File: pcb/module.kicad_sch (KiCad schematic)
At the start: 2 parts, among them J3 Conn_02x07_Counter_Clockwise

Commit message: worked on power
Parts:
- removed A1: RaspberryPi_Pico, Module:RaspberryPi_Pico_SMD_HandSolder, symbol MCU_Module:RaspberryPi_Pico_Debug
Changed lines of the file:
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@@
-		)
-	)
-	(symbol
-		(lib_id "MCU_Module:RaspberryPi_Pico_Debug")
-		(at 210.82 63.5 0)
-		(unit 1)
-		(body_style 1)
-		(exclude_from_sim no)
-		(in_bom yes)
-		(on_board yes)
-		(in_pos_files yes)
-		(dnp no)
-		(fields_autoplaced yes)
-		(property "Reference" "A1"
-			(at 212.9633 97.79 0)
-			(show_name no)
-			(do_not_autoplace no)
-			(effects
-				(font
-					(size 1.27 1.27)
-				)
-				(justify left)
-			)
-		)
-		(property "Value" "RaspberryPi_Pico"
-			(at 212.9633 100.33 0)
-			(show_name no)
-			(do_not_autoplace no)
-			(effects
-				(font
-					(size 1.27 1.27)
-				)
-				(justify left)
-			)
-		)
-		(property "Footprint" "Module:RaspberryPi_Pico_SMD_HandSolder"
-			(at 210.82 110.49 0)
-			(hide yes)
-			(show_name no)
-			(do_not_autoplace no)
-			(effects
-				(font
-					(size 1.27 1.27)
-				)
-			)
-		)
-		(property "Datasheet" "https://datasheets.raspberrypi.com/pico/pico-datasheet.pdf"
-			(at 210.82 113.03 0)
-			(hide yes)
-			(show_name no)
-			(do_not_autoplace no)
-			(effects
-				(font
-					(size 1.27 1.27)
-				)
-			)
-		)
-		(property "Description" "Versatile and inexpensive microcontroller module (with debug pins) powered by RP2040 dual-core Arm Cortex-M0+ processor up to 133 MHz, 264kB SRAM, 2MB QSPI flash; also supports Raspberry Pi Pico 2"
-			(at 210.82 115.57 0)
-			(hide yes)
-			(show_name no)
-			(do_not_autoplace no)
-			(effects
-				(font
-					(size 1.27 1.27)
-				)
-			)
-		)
-		(pin "1"
-		)
-		(pin "2"
-		)
-		(pin "3"
-		)
-		(pin "4"
-		)
-		(pin "5"
-		)
-		(pin "6"
-		)
-		(pin "7"
-		)
-		(pin "8"
-		)
-		(pin "9"
-		)
-		(pin "10"
-		)
-		(pin "11"
-		)
-		(pin "12"
-		)
-		(pin "13"
-		)
-		(pin "14"
-		)
-		(pin "15"
-		)
-		(pin "16"
-		)
-		(pin "17"
-		)
-		(pin "18"
-		)
-		(pin "19"
-		)
-		(pin "20"
-		)
-		(pin "21"
-		)
-		(pin "22"
-		)
-		(pin "23"
-		)
-		(pin "24"
-		)
-		(pin "25"
-		)
-		(pin "26"
-		)
-		(pin "27"
-		)
-		(pin "28"
-		)
-		(pin "29"
-		)
-		(pin "30"
-		)
-		(pin "31"
-		)
-		(pin "32"
-		)
-		(pin "33"
-		)
-		(pin "34"
-		)
-		(pin "35"
-		)
-		(pin "36"
-		)
-		(pin "37"
-		)
-		(pin "38"
-		)
-		(pin "39"
-		)
-		(pin "40"
-		)
-		(pin "D1"
-		)
-		(pin "D2"
-		)
-		(pin "D3"
-		)
-		(instances
-			(project "hackxpansion"
-				(path "/aaf5804d-3f78-442b-969e-39faa388db94/b5240296-cec5-4b31-bcc6-a9044eb67d45"
-					(reference "A1")
-					(unit 1)
-				)
-				(path "/aaf5804d-3f78-442b-969e-39faa388db94/cf2102df-4af4-4ffc-bc4a-65177869e662"
-					(reference "A2")
-					(unit 1)
-				)
-				(path "/aaf5804d-3f78-442b-969e-39faa388db94/e2547c36-86b3-4d0e-a874-a213420fbef7"
-					(reference "A4")
-					(unit 1)
-				)
-				(path "/aaf5804d-3f78-442b-969e-39faa388db94/fee8b4e9-dadd-4cae-a445-acfd08390934"
-					(reference "A3")
-					(unit 1)
-				)
-			)
 		)
 	)

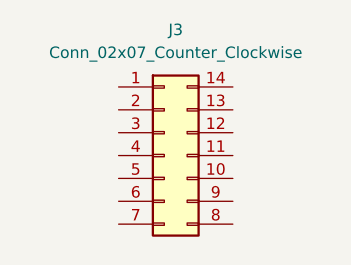
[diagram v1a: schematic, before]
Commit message: updated power sheet, made module female symbol
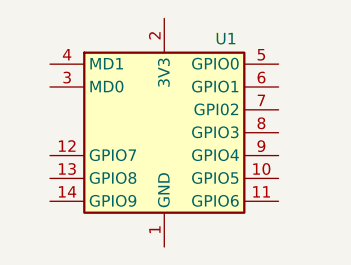
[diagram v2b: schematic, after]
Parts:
- removed J3: Conn_02x07_Counter_Clockwise, Connector_PinSocket_2.54mm:PinSocket_2x07_P2.54mm_Horizontal, symbol Connector_Generic:Conn_02x07_Counter_Clockwise
- added U1: (no value), Connector_PinSocket_2.54mm:PinSocket_2x07_P2.54mm_Horizontal, symbol Hackxpansion:Module_Female
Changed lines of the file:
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@@
 	(paper "A4")
 	(symbol
-		(lib_id "Connector_Generic:Conn_02x07_Counter_Clockwise")
-		(at 128.27 73.66 0)
+		(lib_id "Hackxpansion:Module_Female")
+		(at 128.27 71.12 0)
 		(unit 1)
 		(body_style 1)
@@
 		(in_pos_files yes)
 		(dnp no)
-		(fields_autoplaced yes)
-		(property "Reference" "J3"
-			(at 129.54 59.69 0)
+		(property "Reference" "U1"
+			(at 135.128 60.706 0)
 			(show_name no)
 			(do_not_autoplace no)
@@
 			)
 		)
-		(property "Value" "Conn_02x07_Counter_Clockwise"
-			(at 129.54 62.23 0)
+		(property "Value" ""
+			(at 128.27 71.12 0)
 			(show_name no)
 			(do_not_autoplace no)
@@
 		)
 		(property "Footprint" "Connector_PinSocket_2.54mm:PinSocket_2x07_P2.54mm_Horizontal"
-			(at 128.27 73.66 0)
+			(at 128.27 71.12 0)
 			(hide yes)
 			(show_name no)
@@
 		)
 		(property "Datasheet" ""
-			(at 128.27 73.66 0)
+			(at 128.27 71.12 0)
 			(hide yes)
 			(show_name no)
@@
 			)
 		)
-		(property "Description" "Generic connector, double row, 02x07, counter clockwise pin numbering scheme (similar to DIP package numbering), script generated (kicad-library-utils/schlib/autogen/connector/)"
-			(at 128.27 73.66 0)
+		(property "Description" ""
+			(at 128.27 71.12 0)
 			(hide yes)
 			(show_name no)
@@
 			)
 		)
-		(pin "4"
-		)
-		(pin "10"
-		)
 		(pin "1"
-		)
-		(pin "11"
 		)
 		(pin "3"
@@
 		(pin "2"
 		)
+		(pin "6"
+		)
+		(pin "4"
+		)
+		(pin "5"
+		)
 		(pin "7"
 		)
 		(pin "9"
 		)
-		(pin "12"
+		(pin "13"
 		)
 		(pin "14"
 		)
-		(pin "5"
+		(pin "12"
 		)
-		(pin "13"
+		(pin "11"
+		)
+		(pin "10"
 		)
 		(pin "8"
-		)
-		(pin "6"
 		)
 		(instances
 			(project "hackxpansion"
 				(path "/aaf5804d-3f78-442b-969e-39faa388db94/b5240296-cec5-4b31-bcc6-a9044eb67d45"
-					(reference "J3")
+					(reference "U1")
 					(unit 1)
 				)
 				(path "/aaf5804d-3f78-442b-969e-39faa388db94/cf2102df-4af4-4ffc-bc4a-65177869e662"
-					(reference "J4")
+					(reference "U3")
 					(unit 1)
 				)
 				(path "/aaf5804d-3f78-442b-969e-39faa388db94/e2547c36-86b3-4d0e-a874-a213420fbef7"
-					(reference "J6")
+					(reference "U5")
 					(unit 1)
 				)
 				(path "/aaf5804d-3f78-442b-969e-39faa388db94/fee8b4e9-dadd-4cae-a445-acfd08390934"
-					(reference "J5")
+					(reference "U4")
 					(unit 1)
 				)

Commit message: worked on power
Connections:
- net GND: now reaches U1.1 (GND)
- net GPIO5: now reaches U1.10 (GPIO5)
- net GPIO6: now reaches U1.11 (GPIO6)
- net GPIO7: now reaches U1.12 (GPIO7)
- net GPIO8: now reaches U1.13 (GPIO8)
- net GPIO9: now reaches U1.14 (GPIO9)
- net +3V3: now reaches U1.2 (3V3)
- net mod.MD0: now reaches U1.3 (MD0)
- net mod.MD1: now reaches U1.4 (MD1)
- net GPIO0: now reaches U1.5 (GPIO0)
- net GPIO1: now reaches U1.6 (GPIO1)
- net GPIO2: now reaches U1.7 (GPI02)
- net GPIO3: now reaches U1.8 (GPIO3)
- net GPIO4: now reaches U1.9 (GPIO4)

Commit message: worked on io banks
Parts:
- added R11, R18: 10K, symbol Device:R
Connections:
- net GND: now also R11.2, R18.2
- net mod.MD0 renamed MD0
- net MD0: now also R11.1
- net mod.MD1 renamed MD1
- net MD1: now also R18.1
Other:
- note added: "E24 for the sensing resistors"

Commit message: did a bunch of gpio bank stuff
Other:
- note added: "E24 for the module detect resistors"
- note removed: "E24 for the sensing resistors"
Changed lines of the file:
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@@
 	(generator_version "10.0")
 	(paper "A4")
-	(text "E24 for the sensing resistors"
+	(text "E24 for the module detect resistors"
 		(exclude_from_sim no)
 		(at 167.894 100.33 0)

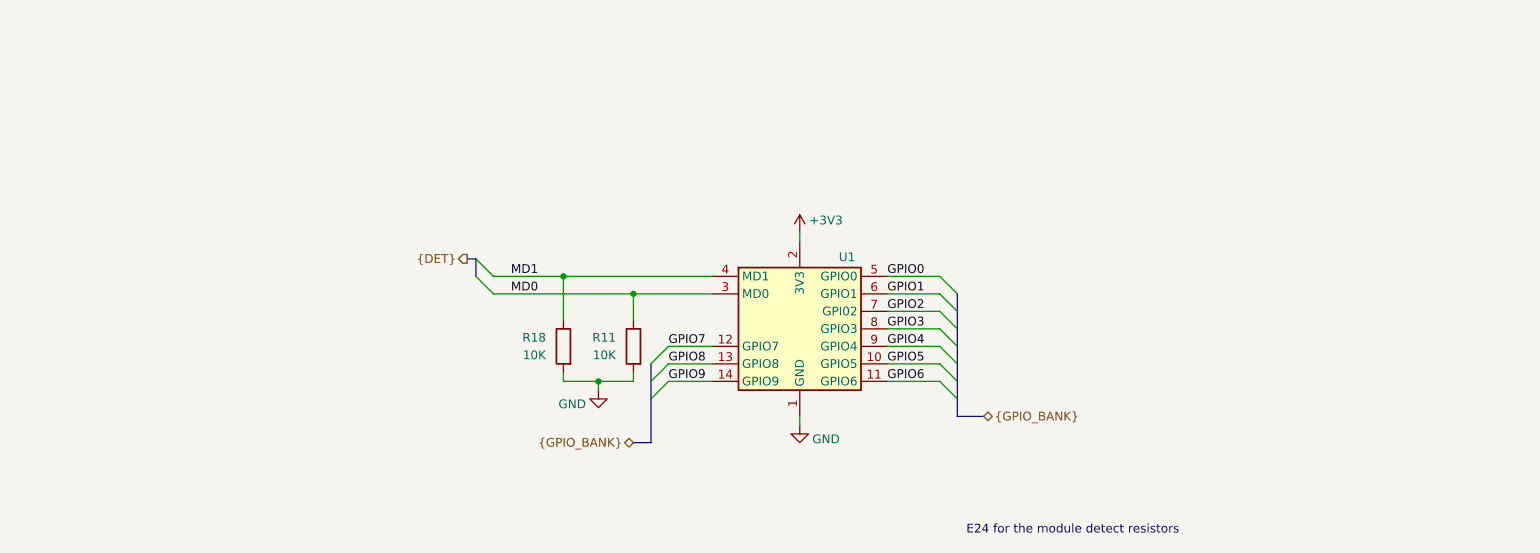
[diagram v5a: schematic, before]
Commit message: started to split up the schematic into two pcbs
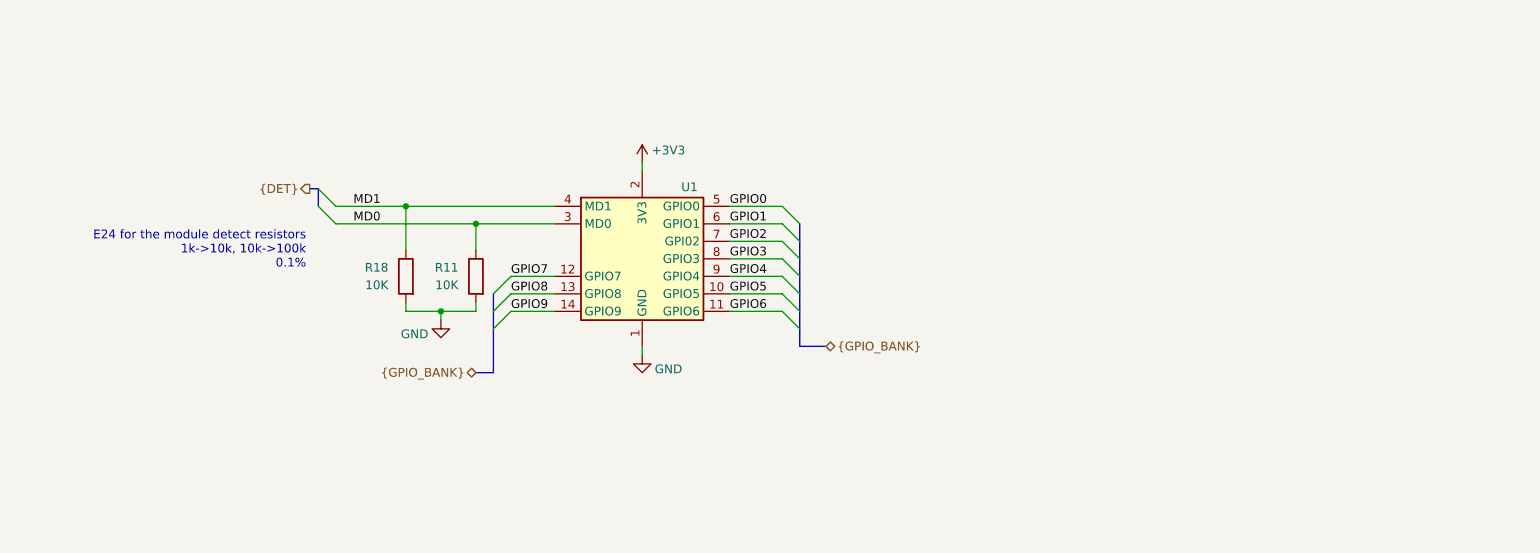
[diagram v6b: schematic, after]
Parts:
- R11, R18: footprint (none) -> Resistor_SMD:R_0402_1005Metric
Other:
- note added: "E24 for the module detect resistors 1k->10k, 10k->100k 0.1%"
- note removed: "E24 for the module detect resistors"
- moved on the sheet: R11, R18, U1

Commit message: reanottad stuff
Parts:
- renumbered R18 to R16
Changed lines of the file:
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@@
 				)
 				(path "/aaf5804d-3f78-442b-969e-39faa388db94/7b3174ee-89a2-4fc3-aea9-d162748ee587/0547b68d-d760-4d9c-a3c3-9a4130f5ea65"
-					(reference "R24")
-					(unit 1)
-				)
-				(path "/aaf5804d-3f78-442b-969e-39faa388db94/7b3174ee-89a2-4fc3-aea9-d162748ee587/82bcf865-3cc6-4dae-b757-27ac9efd6517"
-					(reference "R25")
+					(reference "R20")
+					(unit 1)
+				)
+				(path "/aaf5804d-3f78-442b-969e-39faa388db94/7b3174ee-89a2-4fc3-aea9-d162748ee587/82bcf865-3cc6-4dae-b757-27ac9efd6517"
+					(reference "R21")
 					(unit 1)
 				)
@@
 		(in_pos_files yes)
 		(dnp no)
-		(property "Reference" "R18"
+		(property "Reference" "R16"
 			(at 68.58 62.2299 0)
 			(show_name no)
@@
 			(project "hackxpansion"
 				(path "/aaf5804d-3f78-442b-969e-39faa388db94/61af021d-ad04-487f-9d02-e2b100ecd1ae/83610548-4b56-444f-89db-0bbc742f5add"
+					(reference "R17")
+					(unit 1)
+				)
+				(path "/aaf5804d-3f78-442b-969e-39faa388db94/61af021d-ad04-487f-9d02-e2b100ecd1ae/8e7c9aa8-528d-465c-8c66-453c45c0eb2c"
+					(reference "R16")
+					(unit 1)
+				)
+				(path "/aaf5804d-3f78-442b-969e-39faa388db94/7b3174ee-89a2-4fc3-aea9-d162748ee587/0547b68d-d760-4d9c-a3c3-9a4130f5ea65"
+					(reference "R18")
+					(unit 1)
+				)
+				(path "/aaf5804d-3f78-442b-969e-39faa388db94/7b3174ee-89a2-4fc3-aea9-d162748ee587/82bcf865-3cc6-4dae-b757-27ac9efd6517"
 					(reference "R19")
-					(unit 1)
-				)
-				(path "/aaf5804d-3f78-442b-969e-39faa388db94/61af021d-ad04-487f-9d02-e2b100ecd1ae/8e7c9aa8-528d-465c-8c66-453c45c0eb2c"
-					(reference "R18")
-					(unit 1)
-				)
-				(path "/aaf5804d-3f78-442b-969e-39faa388db94/7b3174ee-89a2-4fc3-aea9-d162748ee587/0547b68d-d760-4d9c-a3c3-9a4130f5ea65"
-					(reference "R22")
-					(unit 1)
-				)
-				(path "/aaf5804d-3f78-442b-969e-39faa388db94/7b3174ee-89a2-4fc3-aea9-d162748ee587/82bcf865-3cc6-4dae-b757-27ac9efd6517"
-					(reference "R23")
 					(unit 1)
 				)
@@
 				)
 				(path "/aaf5804d-3f78-442b-969e-39faa388db94/7b3174ee-89a2-4fc3-aea9-d162748ee587/0547b68d-d760-4d9c-a3c3-9a4130f5ea65"
+					(reference "U4")
+					(unit 1)
+				)
+				(path "/aaf5804d-3f78-442b-969e-39faa388db94/7b3174ee-89a2-4fc3-aea9-d162748ee587/82bcf865-3cc6-4dae-b757-27ac9efd6517"
 					(reference "U6")
 					(unit 1)
 				)
-				(path "/aaf5804d-3f78-442b-969e-39faa388db94/7b3174ee-89a2-4fc3-aea9-d162748ee587/82bcf865-3cc6-4dae-b757-27ac9efd6517"
-					(reference "U8")
-					(unit 1)
-				)
